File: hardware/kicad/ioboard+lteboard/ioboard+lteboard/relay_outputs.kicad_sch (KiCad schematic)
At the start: 23 parts, among them J4 Conn_01x08, K1 ALDP105, K2 ALDP105, K3 ALDP105, K4 ALDP105, Q2 MMBT3904, Q3 MMBT3904, Q4 MMBT3904, Q5 MMBT3904

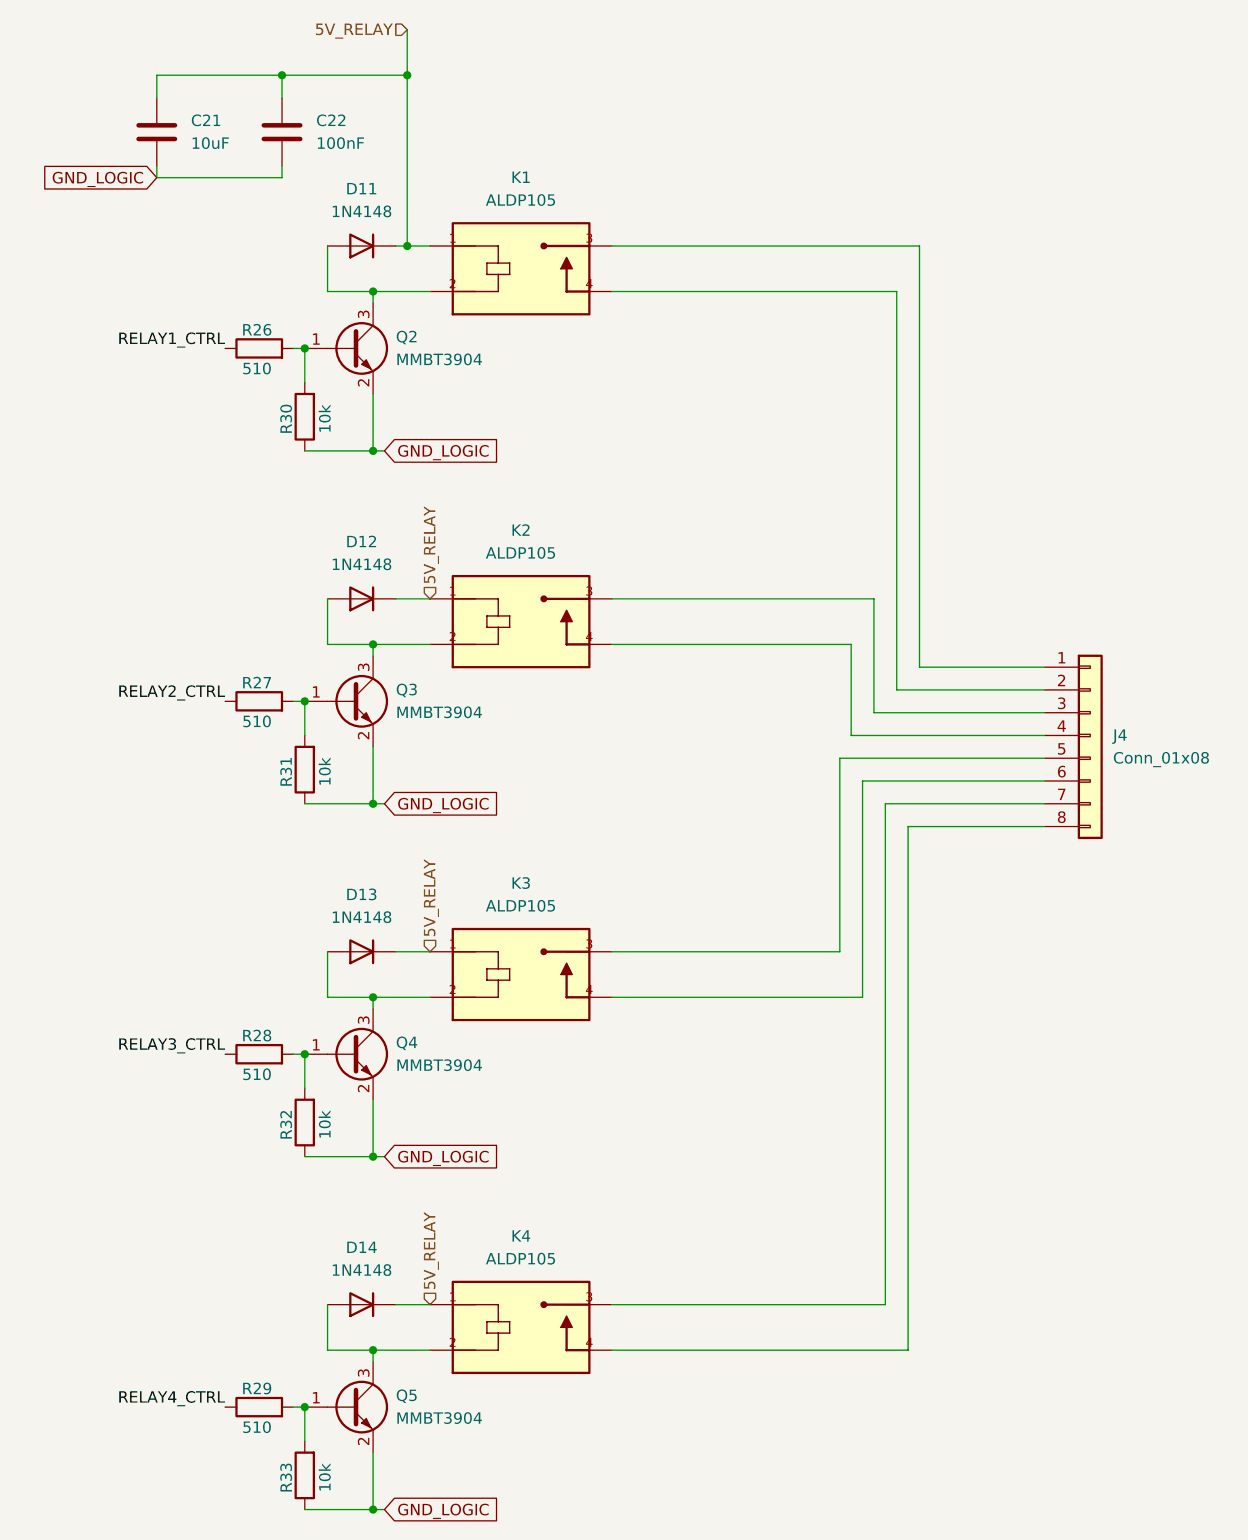
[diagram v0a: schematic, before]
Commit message: added missing hierarchical labels for core-compute, digitil_inputs and relay_output
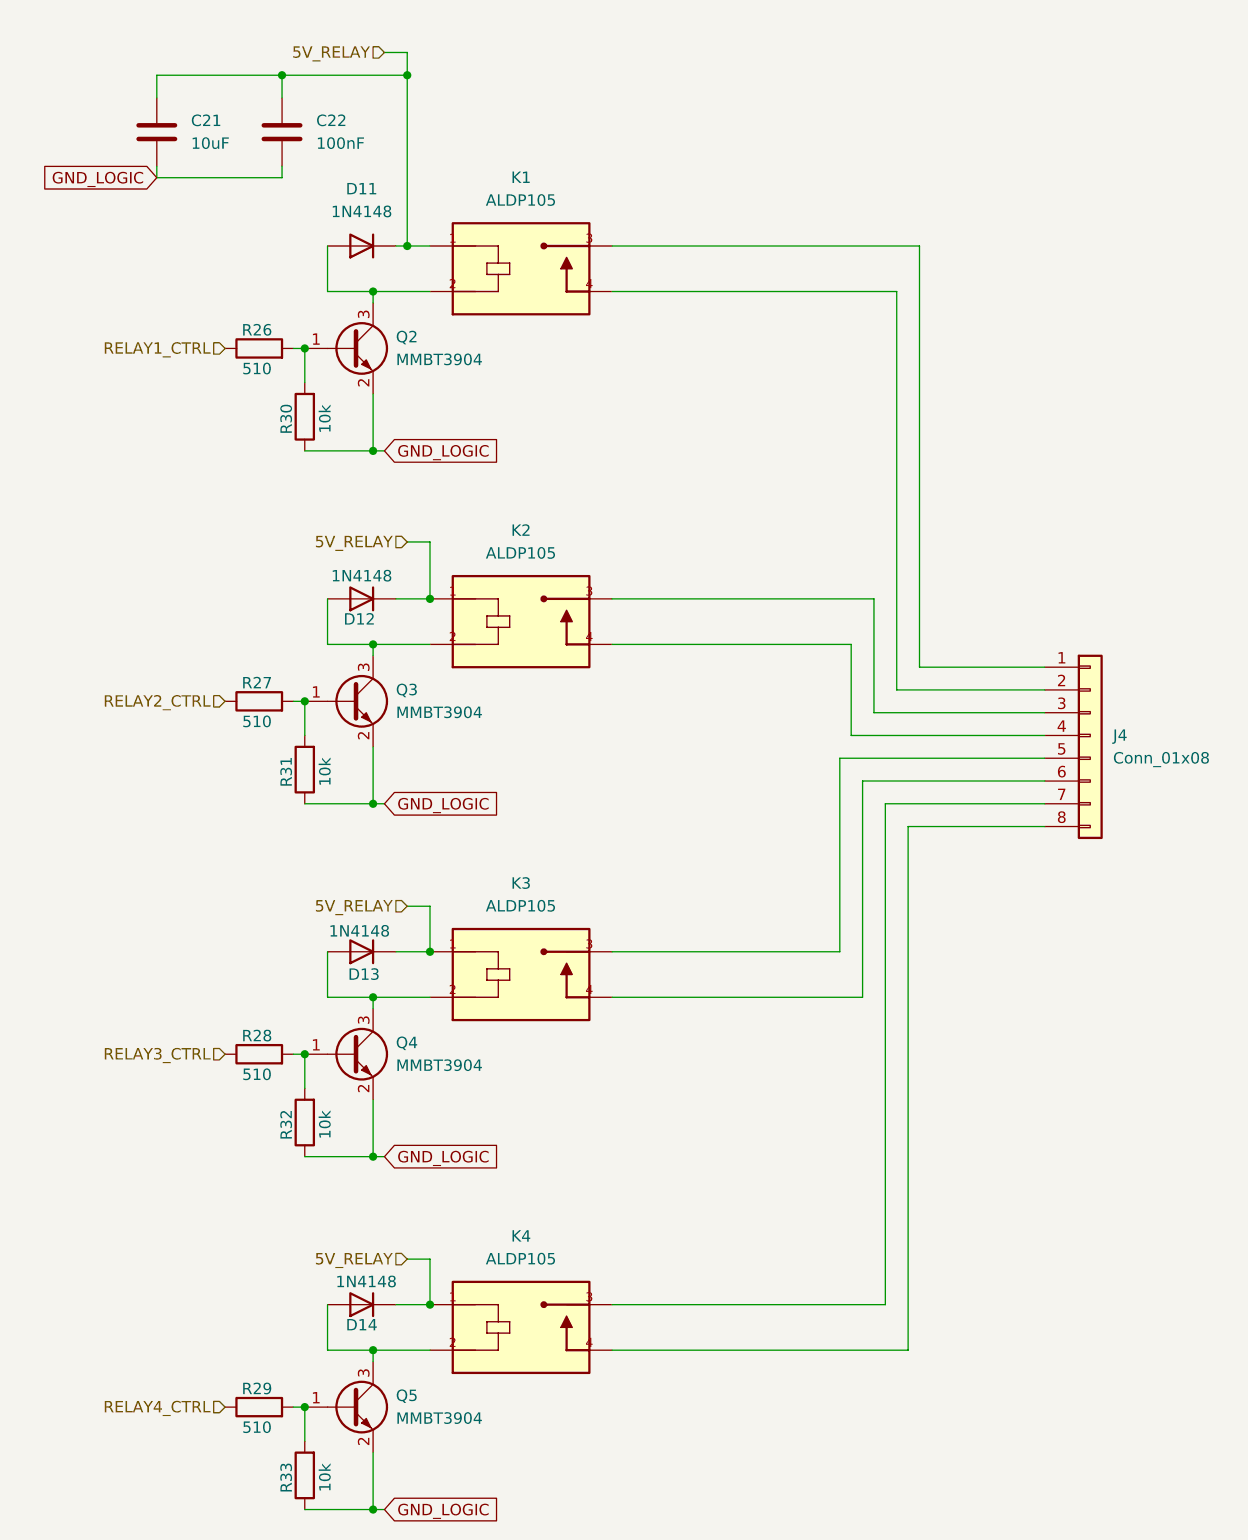
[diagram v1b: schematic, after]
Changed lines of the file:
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@@
 	)
 	(junction
+		(at 78.74 121.92)
+		(diameter 0)
+		(color 0 0 0 0)
+	)
+	(junction
+		(at 78.74 161.29)
+		(diameter 0)
+		(color 0 0 0 0)
+	)
+	(junction
 		(at 64.77 133.35)
 		(diameter 0)
@@
 	)
 	(junction
+		(at 78.74 82.55)
+		(diameter 0)
+		(color 0 0 0 0)
+	)
+	(junction
 		(at 72.39 87.63)
 		(diameter 0)
@@
 	(wire
 		(pts
+			(xy 76.2 76.2) (xy 78.74 76.2)
+		)
+		(stroke
+			(width 0)
+			(type default)
+		)
+	)
+	(wire
+		(pts
+			(xy 76.2 156.21) (xy 78.74 156.21)
+		)
+		(stroke
+			(width 0)
+			(type default)
+		)
+	)
+	(wire
+		(pts
 			(xy 127 102.87) (xy 147.32 102.87)
 		)
@@
 	(wire
 		(pts
+			(xy 78.74 76.2) (xy 78.74 82.55)
+		)
+		(stroke
+			(width 0)
+			(type default)
+		)
+	)
+	(wire
+		(pts
 			(xy 73.66 66.04) (xy 72.39 66.04)
 		)
@@
 	(wire
 		(pts
-			(xy 76.2 19.05) (xy 76.2 24.13)
+			(xy 76.2 21.59) (xy 76.2 24.13)
 		)
 		(stroke
@@
 	(wire
 		(pts
+			(xy 78.74 156.21) (xy 78.74 161.29)
+		)
+		(stroke
+			(width 0)
+			(type default)
+		)
+	)
+	(wire
+		(pts
 			(xy 67.31 48.26) (xy 72.39 48.26)
 		)
@@
 	(wire
 		(pts
+			(xy 76.2 116.84) (xy 78.74 116.84)
+		)
+		(stroke
+			(width 0)
+			(type default)
+		)
+	)
+	(wire
+		(pts
 			(xy 125.73 97.79) (xy 147.32 97.79)
 		)
@@
 	(wire
 		(pts
+			(xy 78.74 116.84) (xy 78.74 121.92)
+		)
+		(stroke
+			(width 0)
+			(type default)
+		)
+	)
+	(wire
+		(pts
+			(xy 73.66 21.59) (xy 76.2 21.59)
+		)
+		(stroke
+			(width 0)
+			(type default)
+		)
+	)
+	(wire
+		(pts
 			(xy 132.08 166.37) (xy 132.08 107.95)
 		)
@@
 		)
 	)
-	(label "RELAY4_CTRL"
-		(at 55.88 172.72 180)
-		(effects
-			(font
-				(size 1.27 1.27)
-			)
-			(justify right bottom)
-		)
-	)
-	(label "RELAY3_CTRL"
-		(at 55.88 133.35 180)
-		(effects
-			(font
-				(size 1.27 1.27)
-			)
-			(justify right bottom)
-		)
-	)
-	(label "RELAY1_CTRL"
-		(at 55.88 54.61 180)
-		(effects
-			(font
-				(size 1.27 1.27)
-			)
-			(justify right bottom)
-		)
-	)
-	(label "RELAY2_CTRL"
-		(at 55.88 93.98 180)
-		(effects
-			(font
-				(size 1.27 1.27)
-			)
-			(justify right bottom)
-		)
-	)
 	(global_label "GND_LOGIC"
 		(shape input)
@@
 		)
 	)
+	(hierarchical_label "RELAY3_CTRL"
+		(shape input)
+		(at 55.88 133.35 180)
+		(effects
+			(font
+				(size 1.27 1.27)
+			)
+			(justify right)
+		)
+	)
+	(hierarchical_label "RELAY1_CTRL"
+		(shape input)
+		(at 55.88 54.61 180)
+		(effects
+			(font
+				(size 1.27 1.27)
+			)
+			(justify right)
+		)
+	)
 	(hierarchical_label "5V_RELAY"
 		(shape input)
-		(at 76.2 19.05 180)
+		(at 73.66 21.59 180)
 		(effects
 			(font
@@
 	(hierarchical_label "5V_RELAY"
 		(shape input)
-		(at 78.74 121.92 90)
+		(at 76.2 116.84 180)
 		(effects
 			(font
 				(size 1.27 1.27)
 			)
-			(justify left)
+			(justify right)
 		)
 	)
 	(hierarchical_label "5V_RELAY"
 		(shape input)
-		(at 78.74 82.55 90)
+		(at 76.2 76.2 180)
 		(effects
 			(font
 				(size 1.27 1.27)
 			)
-			(justify left)
+			(justify right)
 		)
 	)
 	(hierarchical_label "5V_RELAY"
 		(shape input)
-		(at 78.74 161.29 90)
+		(at 76.2 156.21 180)
 		(effects
 			(font
 				(size 1.27 1.27)
 			)
-			(justify left)
+			(justify right)
+		)
+	)
+	(hierarchical_label "RELAY2_CTRL"
+		(shape input)
+		(at 55.88 93.98 180)
+		(effects
+			(font
+				(size 1.27 1.27)
+			)
+			(justify right)
+		)
+	)
+	(hierarchical_label "RELAY4_CTRL"
+		(shape input)
+		(at 55.88 172.72 180)
+		(effects
+			(font
+				(size 1.27 1.27)
+			)
+			(justify right)
 		)
 	)
@@
 		(on_board yes)
 		(dnp no)
-		(fields_autoplaced yes)
 		(property "Reference" "D14"
-			(at 71.12 154.94 0)
+			(at 71.12 163.576 0)
 			(effects
 				(font
@@
 		)
 		(property "Value" "1N4148"
-			(at 71.12 157.48 0)
+			(at 71.628 158.75 0)
 			(effects
 				(font
@@
 		(on_board yes)
 		(dnp no)
-		(fields_autoplaced yes)
 		(property "Reference" "D13"
-			(at 71.12 115.57 0)
+			(at 71.374 124.46 0)
 			(effects
 				(font
@@
 		)
 		(property "Value" "1N4148"
-			(at 71.12 118.11 0)
+			(at 70.866 119.634 0)
 			(effects
 				(font
@@
 		(on_board yes)
 		(dnp no)
-		(fields_autoplaced yes)
 		(property "Reference" "D12"
-			(at 71.12 76.2 0)
+			(at 70.866 84.836 0)
 			(effects
 				(font
@@
 		)
 		(property "Value" "1N4148"
-			(at 71.12 78.74 0)
+			(at 71.12 80.01 0)
 			(effects
 				(font
